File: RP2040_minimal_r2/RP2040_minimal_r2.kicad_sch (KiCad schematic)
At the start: 33 parts, among them J1 SPI0.6, J2 SPI0.8, J3 SPI1.13, J5 USB, SW1 BOOT, SW2 RESET, U1 AP2112K-3.3TRG1, U2 W25Q128JVS, U3 RP2040, Y1 X322512MSB4SI

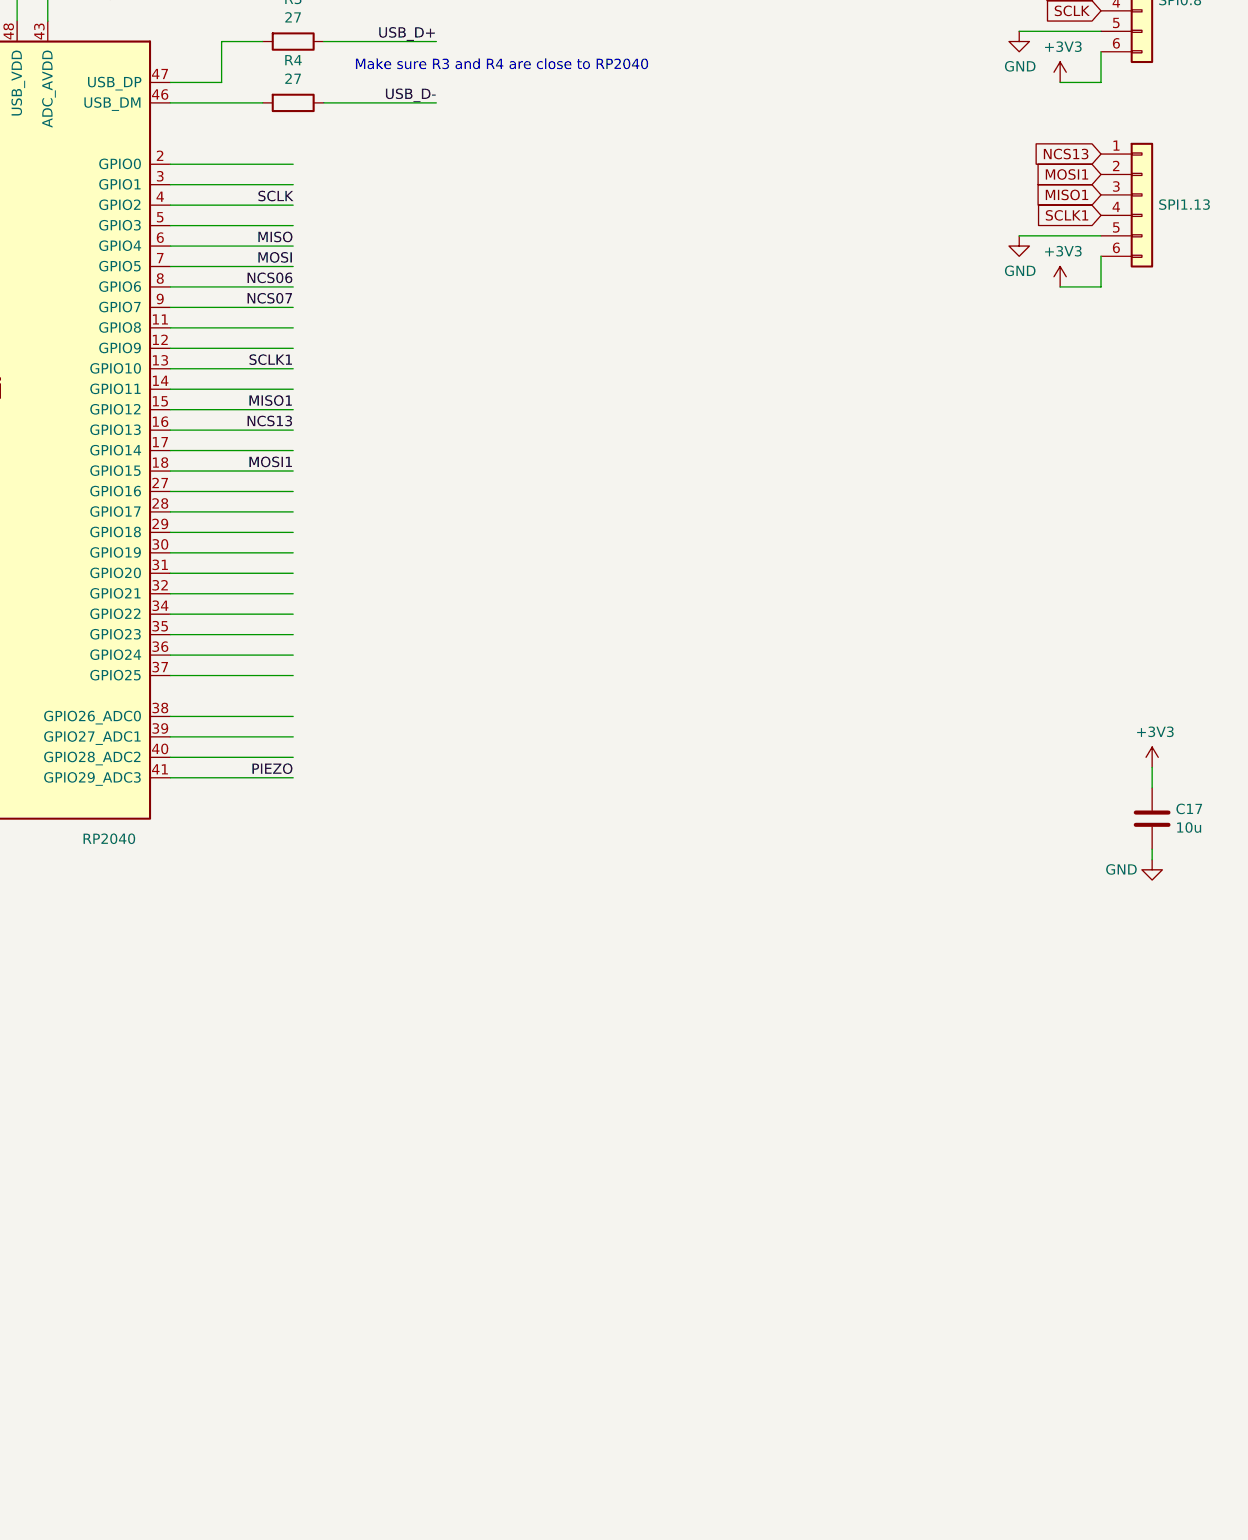
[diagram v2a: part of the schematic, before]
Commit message: Add I2C/STEMMA QT connector
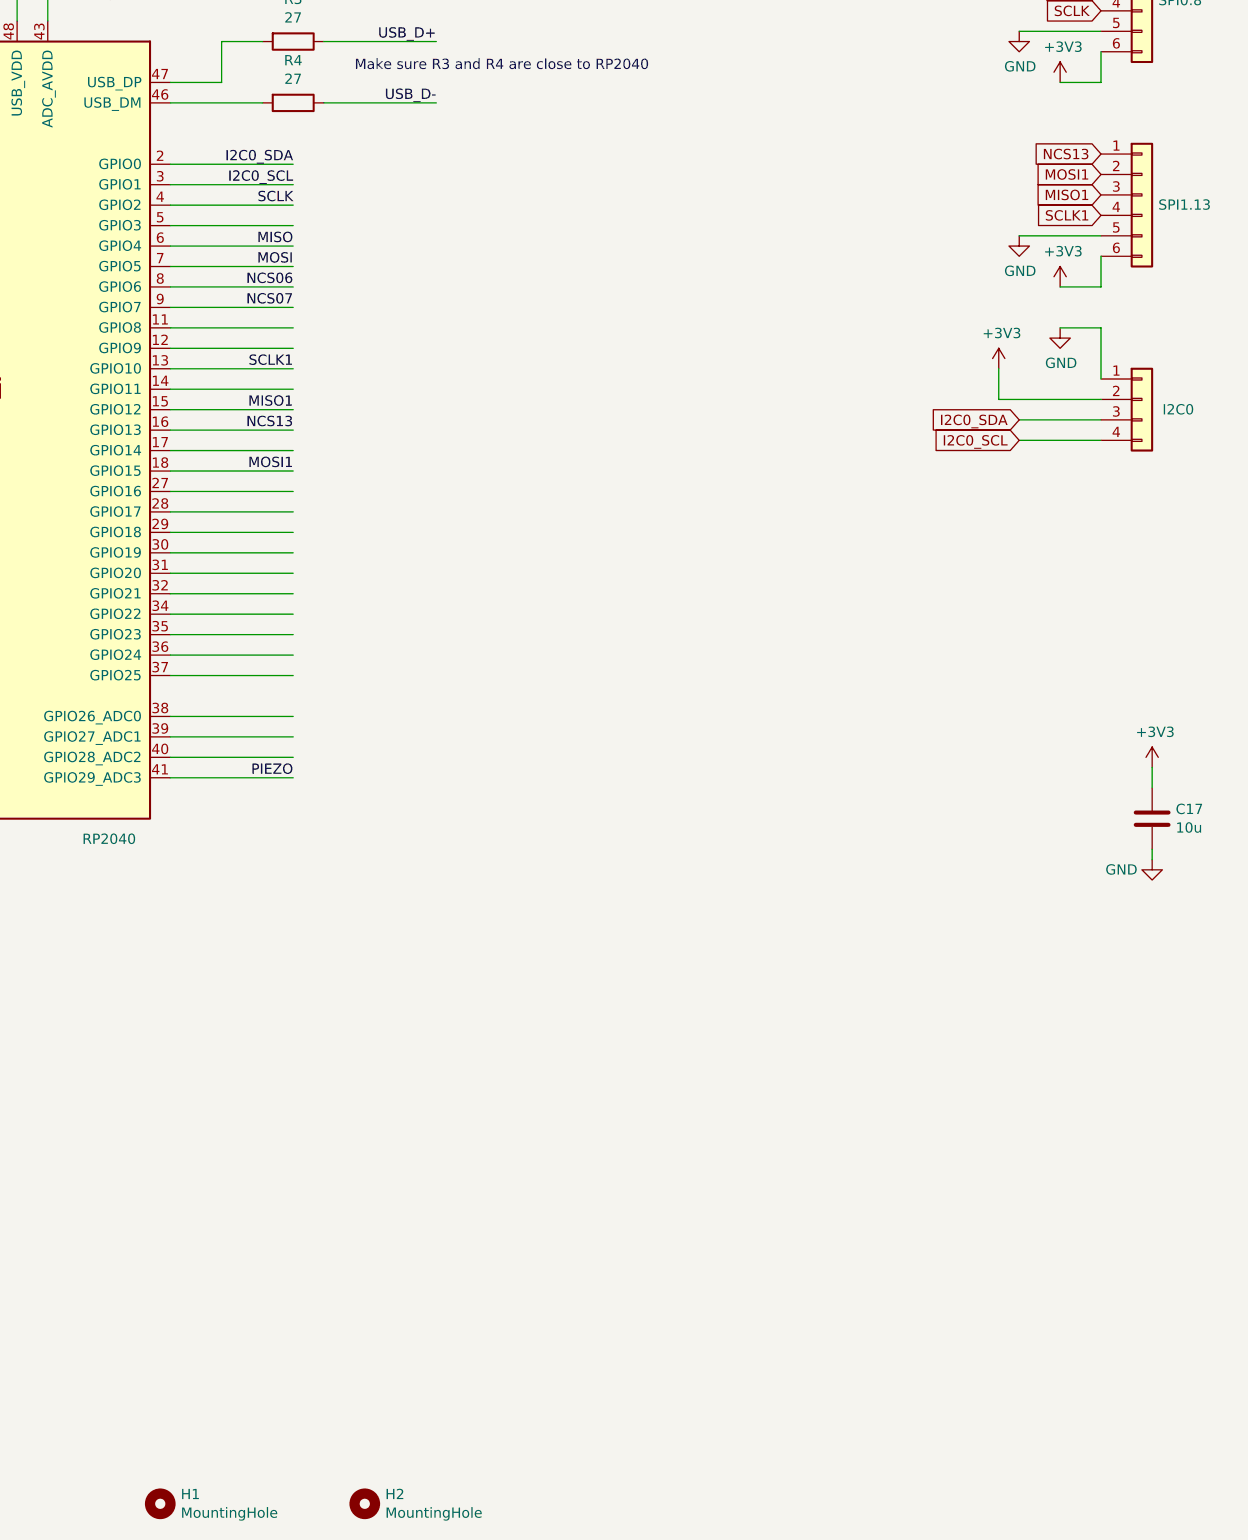
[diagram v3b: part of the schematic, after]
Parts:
- added H1, H2: MountingHole, MountingHole:MountingHole_2.2mm_M2, symbol Mechanical:MountingHole
- added J4: I2C0, Connector_JST:JST_SH_BM04B-SRSS-TB_1x04-1MP_P1.00mm_Vertical, symbol Connector_Generic:Conn_01x04
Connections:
- net +3V3: now also J4.2 (Pin_2)
- net GND: now also J4.1 (Pin_1)
- net I2C0_SDA: now reaches U3.2 (GPIO0)
- net I2C0_SDA: now also J4.3 (Pin_3)
- net I2C0_SCL: now reaches U3.3 (GPIO1)
- net I2C0_SCL: now also J4.4 (Pin_4)

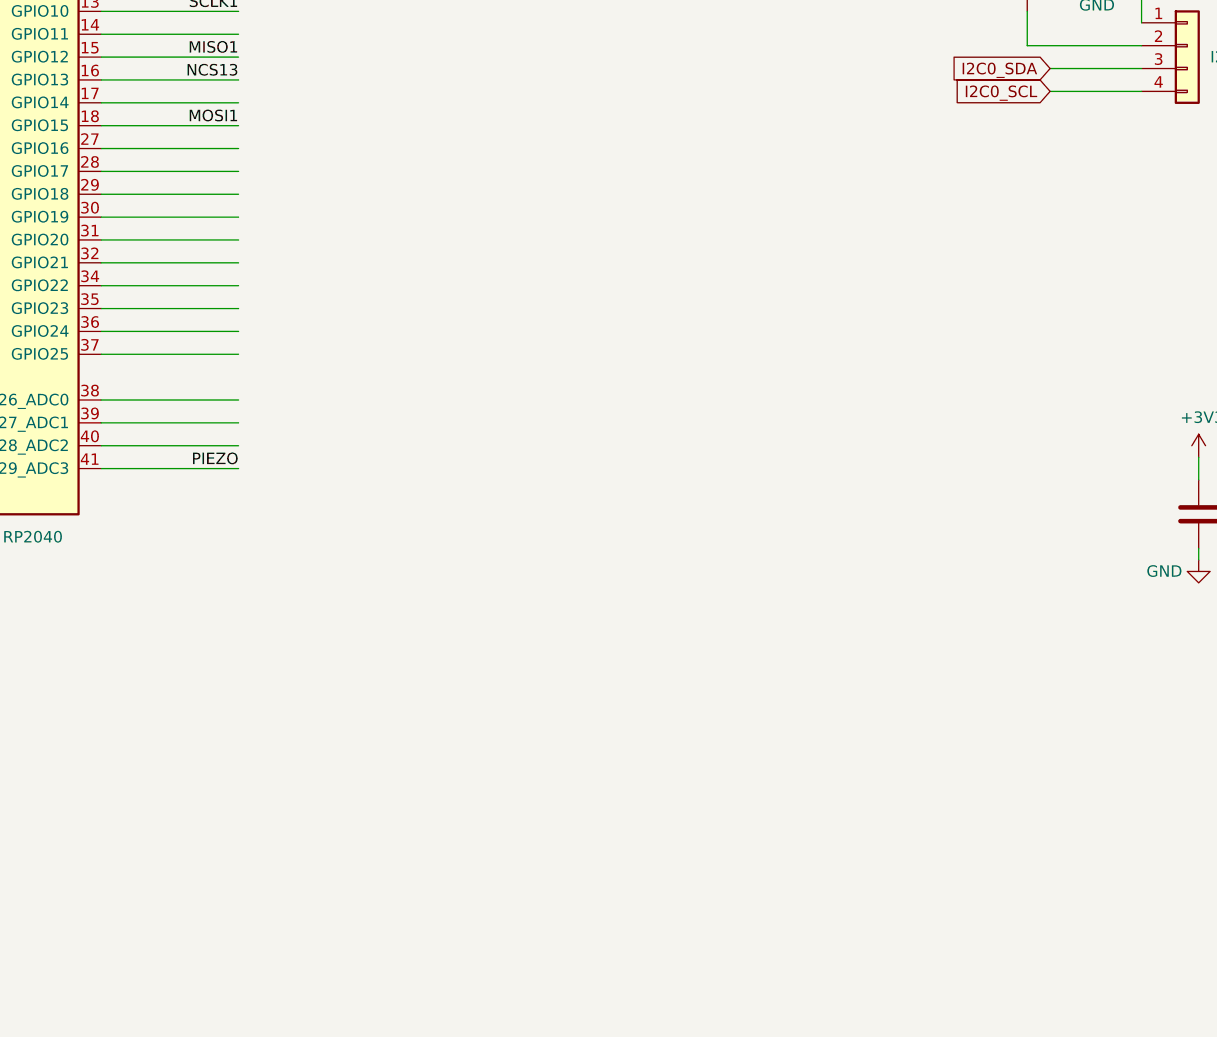
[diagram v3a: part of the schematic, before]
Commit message: Added 6 button connectors. Added 6 pin breakout for GPIO 26-29 (includes ground and +3.3v as well).
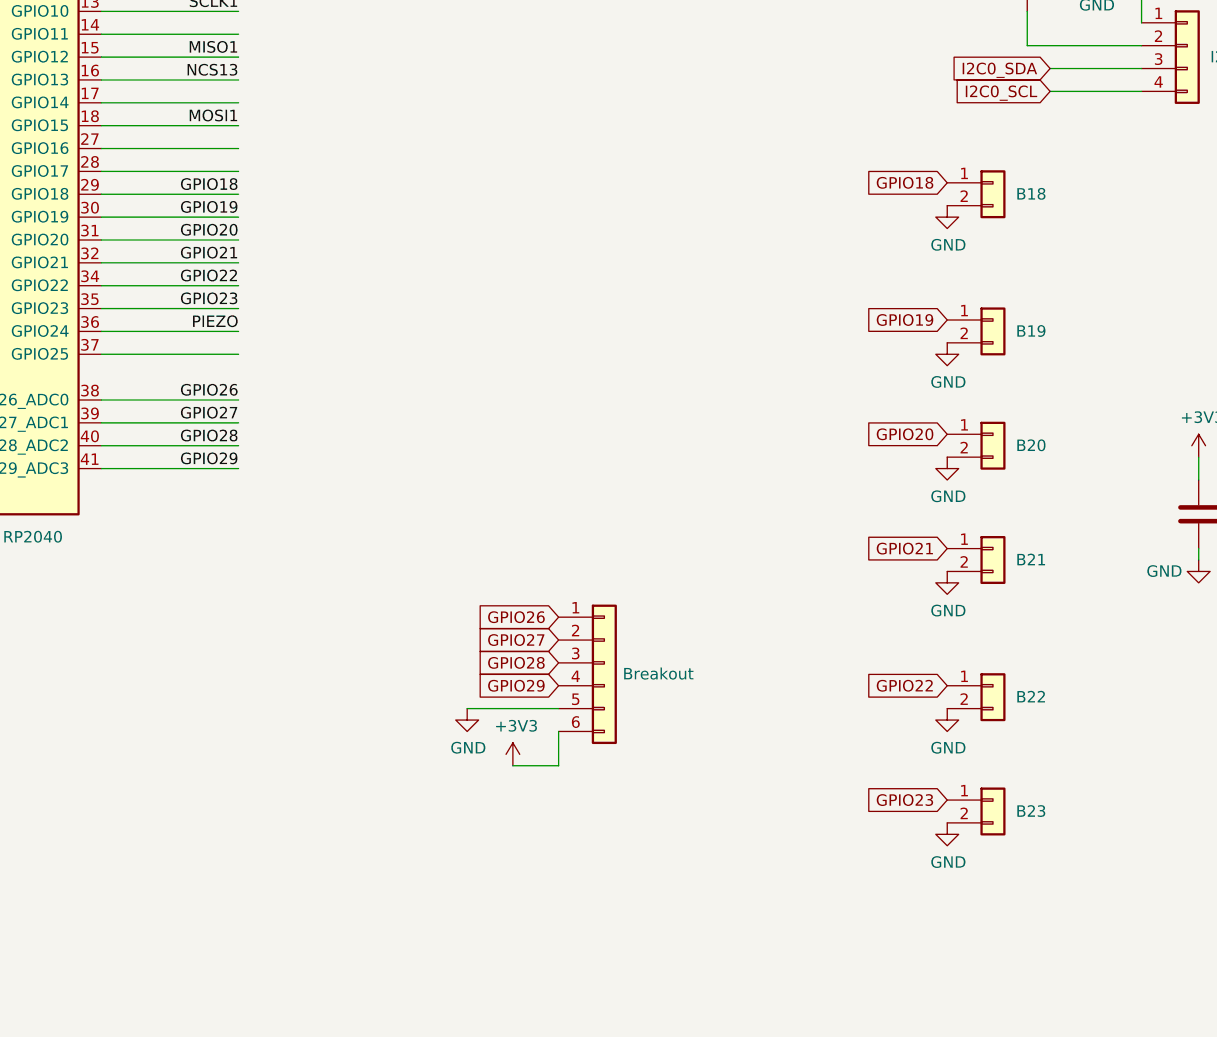
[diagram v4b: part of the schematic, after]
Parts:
- added J10: B22, Connector_JST:JST_SH_BM02B-SRSS-TB_1x02-1MP_P1.00mm_Vertical, symbol Connector_Generic:Conn_01x02
- added J11: B23, Connector_JST:JST_SH_BM02B-SRSS-TB_1x02-1MP_P1.00mm_Vertical, symbol Connector_Generic:Conn_01x02
- added J12: Breakout, Connector_JST:JST_SH_BM06B-SRSS-TB_1x06-1MP_P1.00mm_Vertical, symbol Connector_Generic:Conn_01x06
- added J6: B18, Connector_JST:JST_SH_BM02B-SRSS-TB_1x02-1MP_P1.00mm_Vertical, symbol Connector_Generic:Conn_01x02
- added J7: B19, Connector_JST:JST_SH_BM02B-SRSS-TB_1x02-1MP_P1.00mm_Vertical, symbol Connector_Generic:Conn_01x02
- added J8: B20, Connector_JST:JST_SH_BM02B-SRSS-TB_1x02-1MP_P1.00mm_Vertical, symbol Connector_Generic:Conn_01x02
- added J9: B21, Connector_JST:JST_SH_BM02B-SRSS-TB_1x02-1MP_P1.00mm_Vertical, symbol Connector_Generic:Conn_01x02
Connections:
- net +3V3: now also J12.6 (Pin_6)
- net GND: now also J10.2 (Pin_2), J11.2 (Pin_2), J12.5 (Pin_5), J6.2 (Pin_2), J7.2 (Pin_2), J8.2 (Pin_2), J9.2 (Pin_2)
- net PIEZO: now also U3.36 (GPIO24); no longer U3.41 (GPIO29_ADC3)
- net GPIO18: now reaches U3.29 (GPIO18)
- net GPIO18: now also J6.1 (Pin_1)
- net GPIO19: now reaches U3.30 (GPIO19)
- net GPIO19: now also J7.1 (Pin_1)
- net GPIO20: now reaches U3.31 (GPIO20)
- net GPIO20: now also J8.1 (Pin_1)
- net GPIO21: now reaches U3.32 (GPIO21)
- net GPIO21: now also J9.1 (Pin_1)
- net GPIO22: now reaches U3.34 (GPIO22)
- net GPIO22: now also J10.1 (Pin_1)
- net GPIO23: now reaches U3.35 (GPIO23)
- net GPIO23: now also J11.1 (Pin_1)
- net GPIO26: now reaches U3.38 (GPIO26_ADC0)
- net GPIO26: now also J12.1 (Pin_1)
- net GPIO27: now reaches U3.39 (GPIO27_ADC1)
- net GPIO27: now also J12.2 (Pin_2)
- net GPIO28: now reaches U3.40 (GPIO28_ADC2)
- net GPIO28: now also J12.3 (Pin_3)
- new net GPIO29: J12.4 (Pin_4), U3.41 (GPIO29_ADC3)

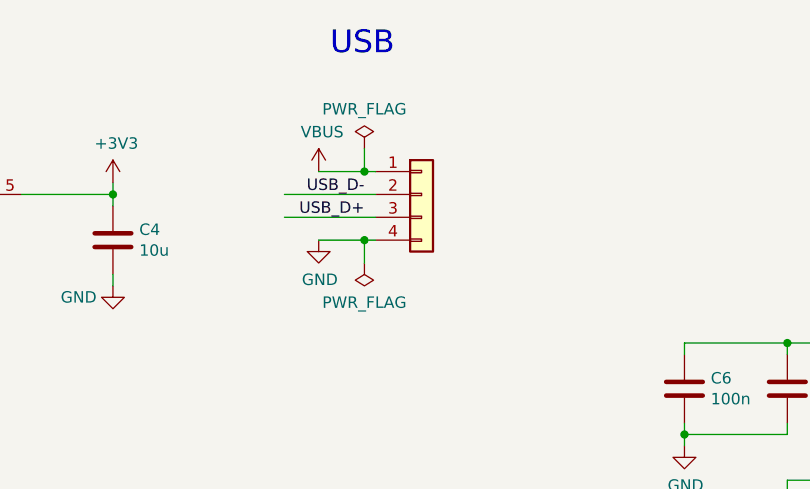
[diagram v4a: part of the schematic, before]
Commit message: Update gerbers and BOM/placement files. Add readme file. Add github url to rear silkscreen layer. Clean up some old unused fill zones that I'd moved off to the side.
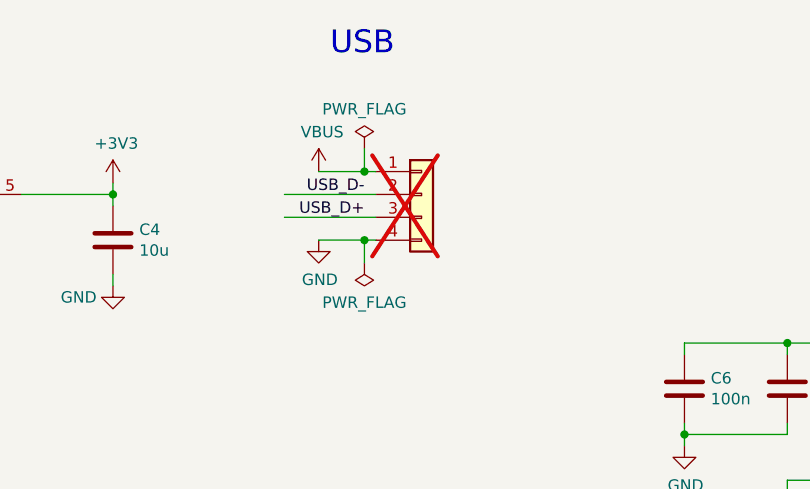
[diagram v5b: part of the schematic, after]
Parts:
- J10, J11, J6, J7, J8, J9: LCSC (none) -> C160388
- J4: LCSC (none) -> C160390
- J5: now not fitted
- SW1, SW2: LCSC C271750 -> C231329
- U2: LCSC C97521 -> C190862
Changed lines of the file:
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@@
 			)
 		)
-		(property "LCSC" "C97521"
+		(property "LCSC" "C190862"
 			(at 97.79 133.35 0)
 			(effects
@@
 			)
 		)
-		(property "LCSC" "C271750"
+		(property "LCSC" "C231329"
 			(at 147.32 165.1 0)
 			(effects
@@
 			)
 		)
+		(property "LCSC" "C160388"
+			(at 328.93 184.15 0)
+			(effects
+				(font
+					(size 1.27 1.27)
+				)
+				(hide yes)
+			)
+		)
 		(pin "2"
 		)
@@
 		(in_bom yes)
 		(on_board yes)
-		(dnp no)
+		(dnp yes)
 		(property "Reference" "J5"
 			(at 130.302 44.6532 0)
@@
 			)
 		)
+		(property "LCSC" "C160390"
+			(at 350.52 140.97 0)
+			(effects
+				(font
+					(size 1.27 1.27)
+				)
+				(hide yes)
+			)
+		)
 		(pin "4"
 		)
@@
 			)
 		)
-		(property "LCSC" "C271750"
+		(property "LCSC" "C231329"
 			(at 39.37 125.73 0)
 			(effects
@@
 			)
 		)
+		(property "LCSC" "C160388"
+			(at 328.93 196.85 0)
+			(effects
+				(font
+					(size 1.27 1.27)
+				)
+				(hide yes)
+			)
+		)
 		(pin "2"
 		)
@@
 			)
 		)
+		(property "LCSC" "C160388"
+			(at 328.93 171.45 0)
+			(effects
+				(font
+					(size 1.27 1.27)
+				)
+				(hide yes)
+			)
+		)
 		(pin "2"
 		)
@@
 			)
 		)
+		(property "LCSC" "C160388"
+			(at 328.93 212.09 0)
+			(effects
+				(font
+					(size 1.27 1.27)
+				)
+				(hide yes)
+			)
+		)
 		(pin "2"
 		)
@@
 			)
 		)
+		(property "LCSC" "C160388"
+			(at 328.93 224.79 0)
+			(effects
+				(font
+					(size 1.27 1.27)
+				)
+				(hide yes)
+			)
+		)
 		(pin "2"
 		)
@@
 			(at 328.93 156.21 0)
 			(effects
+				(font
+					(size 1.27 1.27)
+				)
+				(hide yes)
+			)
+		)
+		(property "LCSC" "C160388"
+			(at 328.93 156.21 0)
+			(effects
